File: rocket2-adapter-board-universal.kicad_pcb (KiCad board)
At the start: 2 copper layers, 45 x 55 mm, 13 parts, among them J2 Conn_01x04_Socket, J3 Conn_01x02_Socket, J4 Conn_01x04_Socket, J5 DSUB_15pin/VGA Veritical Fema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

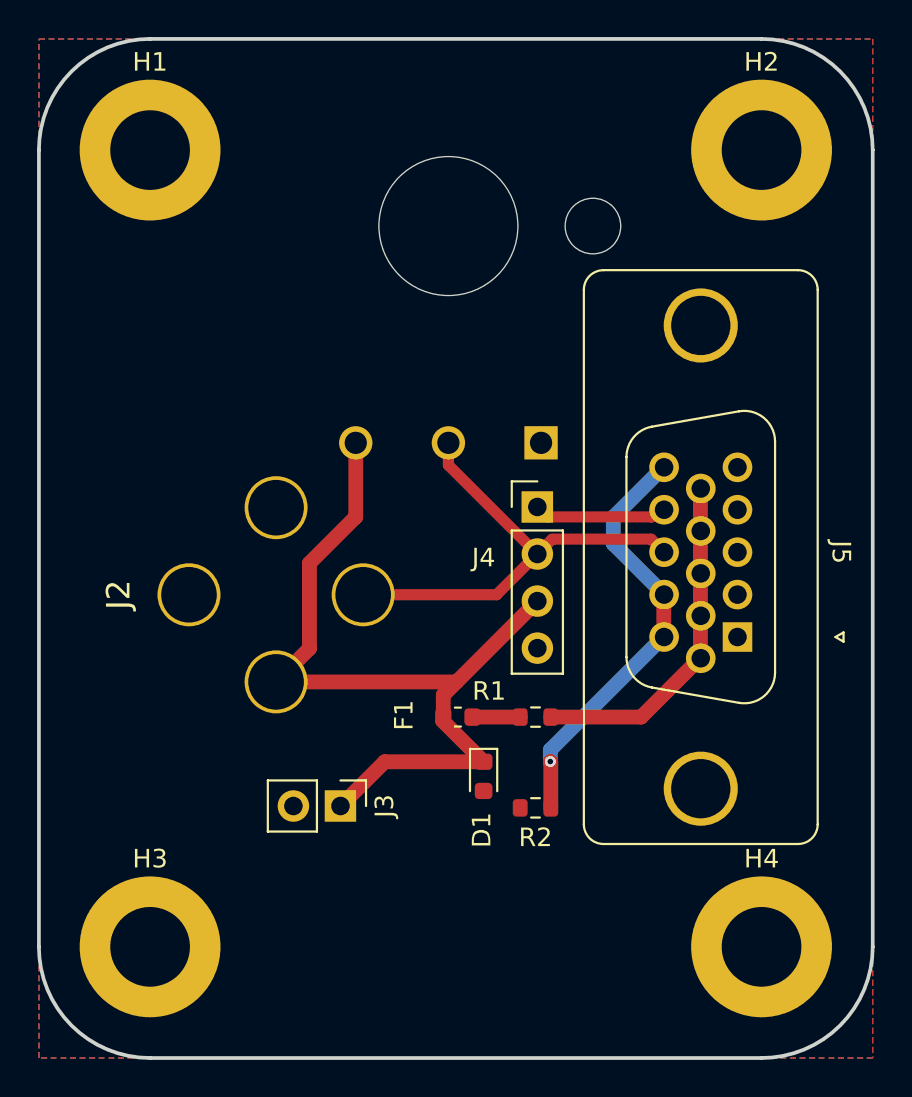
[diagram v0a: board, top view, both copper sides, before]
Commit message: Layout Update 2 + DSUB & Footprint Fixes
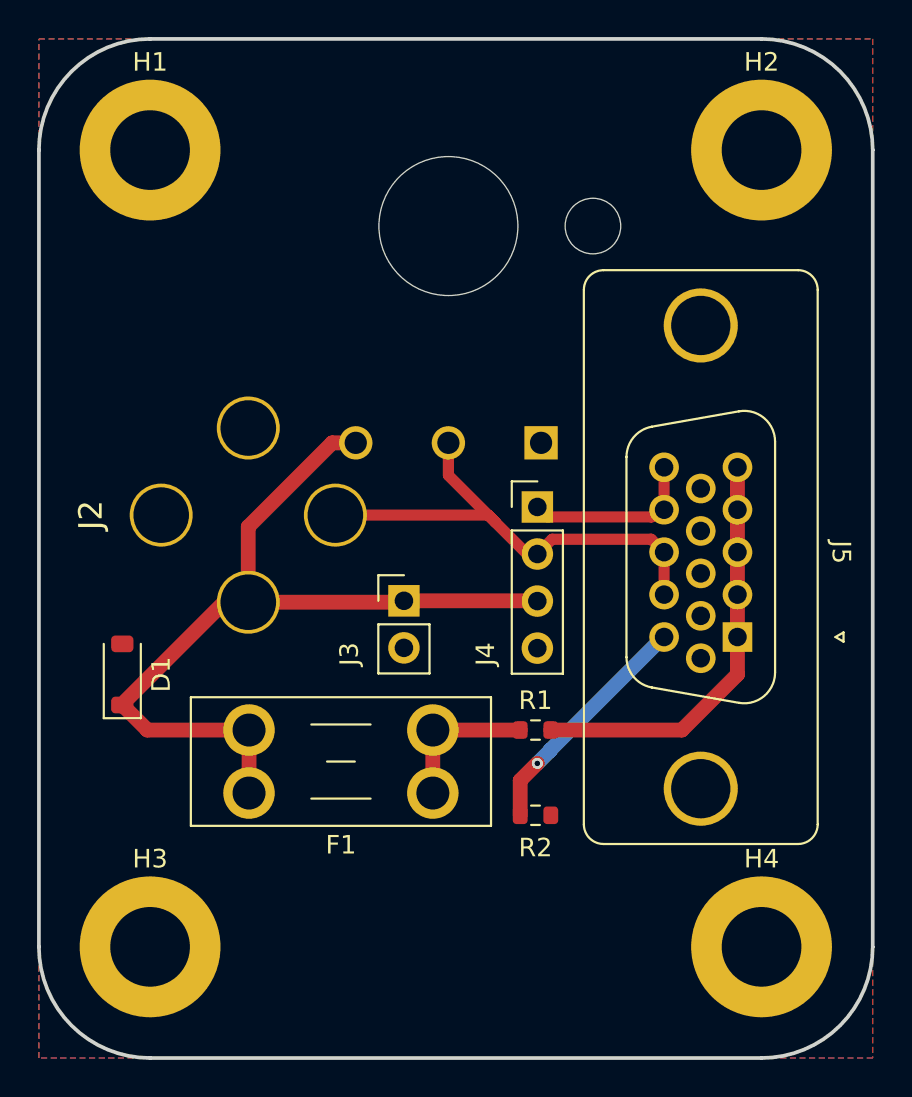
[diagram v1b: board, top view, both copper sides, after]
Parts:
- D1: footprint Diode_SMD:D_0603_1608Metric -> Diode_SMD:D_SOD-123
- F1: footprint Fuse:Fuse_0603_1608Metric -> Fuse:Fuseholder_Blade_Mini_Keystone_3568
- moved D1 20.3 mm to (124.5, 94.3), turned to 90 degrees
- moved J3 11.6 mm to (139.7, 90.3), turned to 0 degrees
- moved J2 4.55 mm to (131.3, 85.7)
- moved F1 4.32 mm to (141.3, 100.7)
- moved R1 0.70 mm to (146.8, 97.3)
- moved R2 0.40 mm to (146.8, 101.9), turned to 180 degrees
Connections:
- J5 pad 0: GND -> CHASSIS GND
- J5 pad 1: GND -> VIN
- J5 pad 10: VIN -> GND
- J5 pad 12: Net-(J5-Pad11) -> AIN+
- J5 pad 15: Net-(J5-Pad11) -> AIN-
- J5 pad 2: GND -> VIN
- J5 pad 3: GND -> VIN
- J5 pad 4: GND -> VIN
- J5 pad 5: GND -> VIN
- J5 pad 6: VIN -> GND
- J5 pad 7: VIN -> GND
- J5 pad 8: VIN -> GND
- J5 pad 9: VIN -> GND
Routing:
- net Net-(J5-Pad11): track 23.2 -> 12.9 mm
- net Net-(F1-Pad1): track 2.57 -> 8.15 mm
- net VIN: track 18.6 -> 22.5 mm
- net VBUS: track 44.8 -> 47.4 mm
- net AIN-: track 7.32 -> 9.61 mm
- net AIN+: track 25.9 -> 27.0 mm

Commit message: Layout Return Paths Fix
Streamlined GND return paths
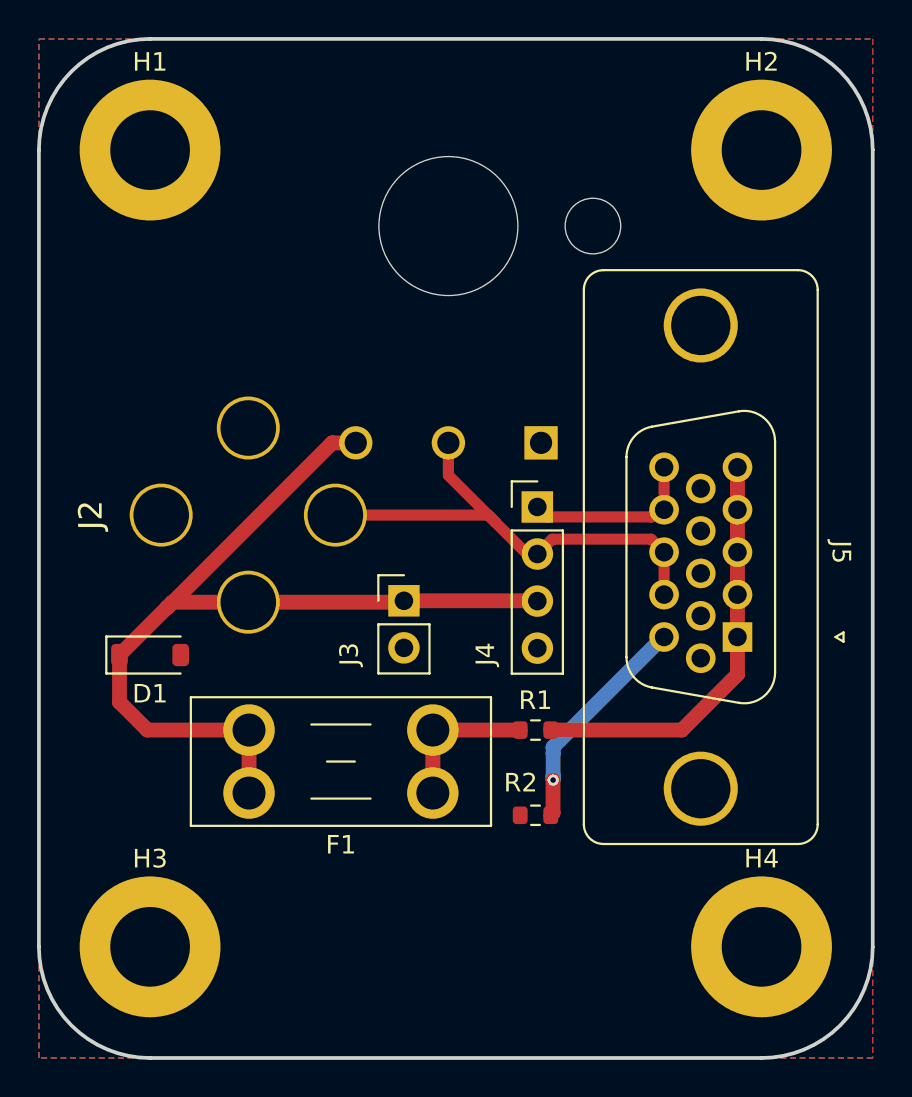
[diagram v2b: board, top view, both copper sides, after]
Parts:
- moved D1 1.83 mm to (126.0, 93.2), turned to 0 degrees
- turned R2 to 0 degrees
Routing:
- net VBUS: track 47.4 -> 51.2 mm

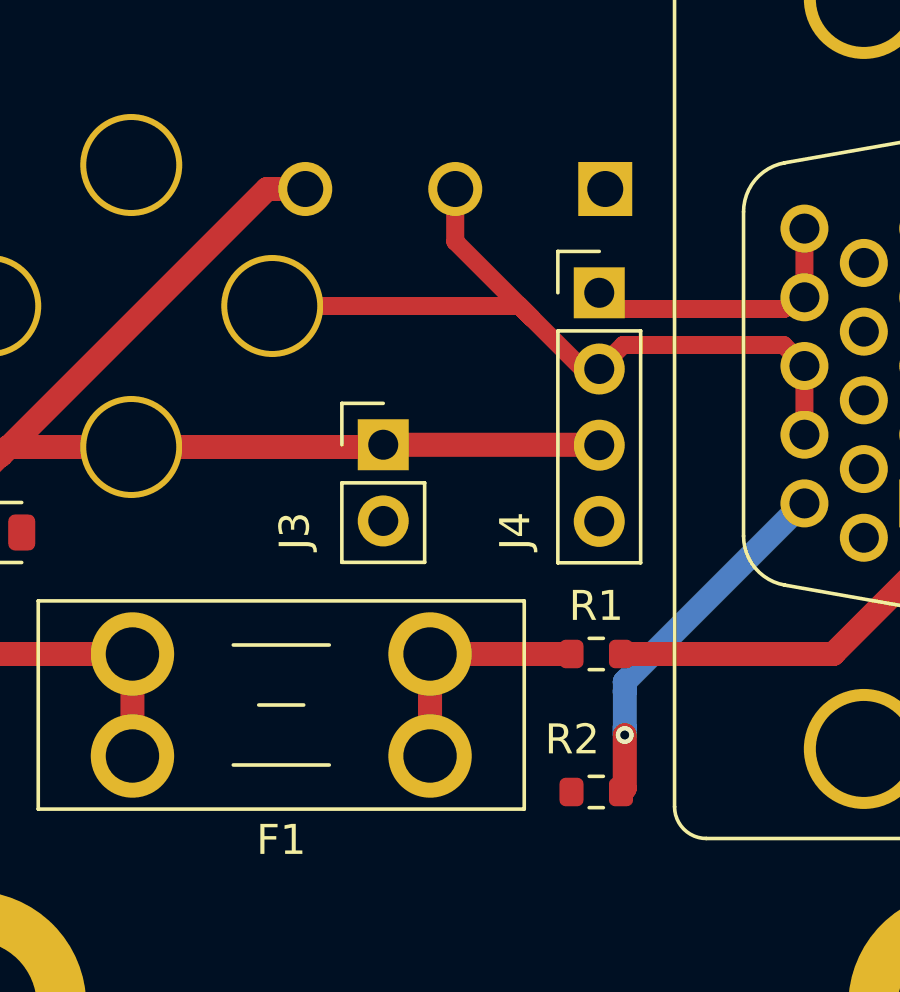
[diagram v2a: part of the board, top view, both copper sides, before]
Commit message: Layout Update 3 + Schematic Links & DSUB Update
Added R2 to bridge AIN+ and AIN-
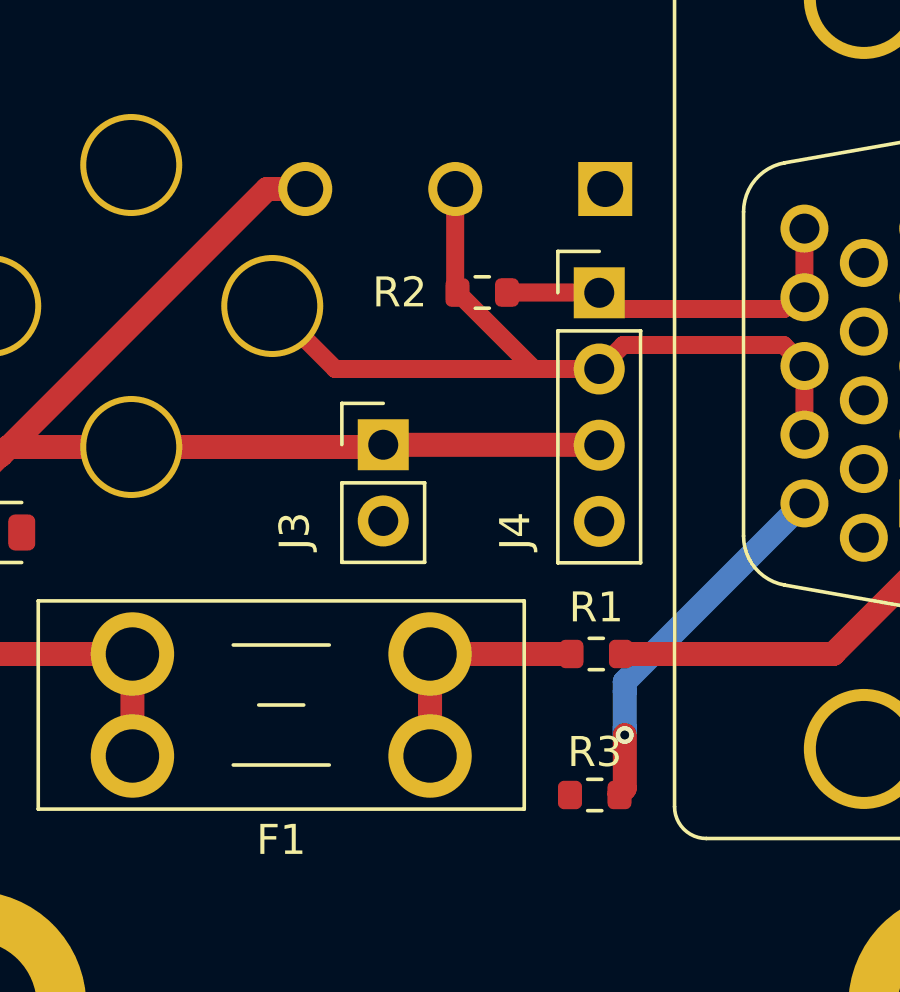
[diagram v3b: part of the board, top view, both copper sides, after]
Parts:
- added R3: 10k, Resistor_SMD:R_0603_1608Metric, F.Cu at (146.8, 102.0)
- R2: value 10k -> 0
- moved R2 17.1 mm to (143.0, 85.2), turned to 180 degrees
- turned R1 to 0 degrees
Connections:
- R1 pad 1: VIN -> Net-(F1-Pad1)
- R1 pad 2: Net-(F1-Pad1) -> VIN
- R2 pad 1: GND -> AIN-
- R2 pad 2: Net-(J5-Pad11) -> AIN+
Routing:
- net AIN+: track 27.0 -> 30.9 mm
- net AIN-: track 9.61 -> 12.7 mm

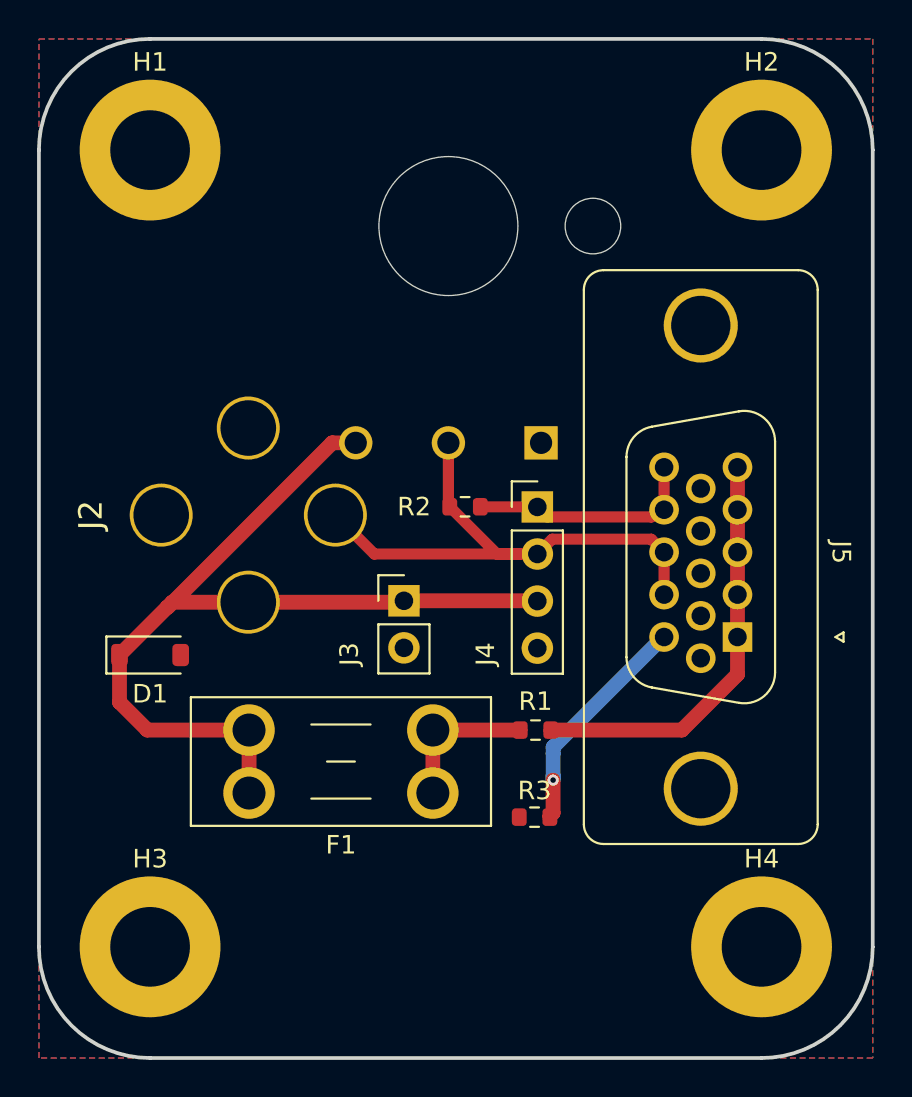
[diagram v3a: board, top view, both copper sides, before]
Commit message: Layout Update 4: NC pins, PT and Solenoid pad fixes
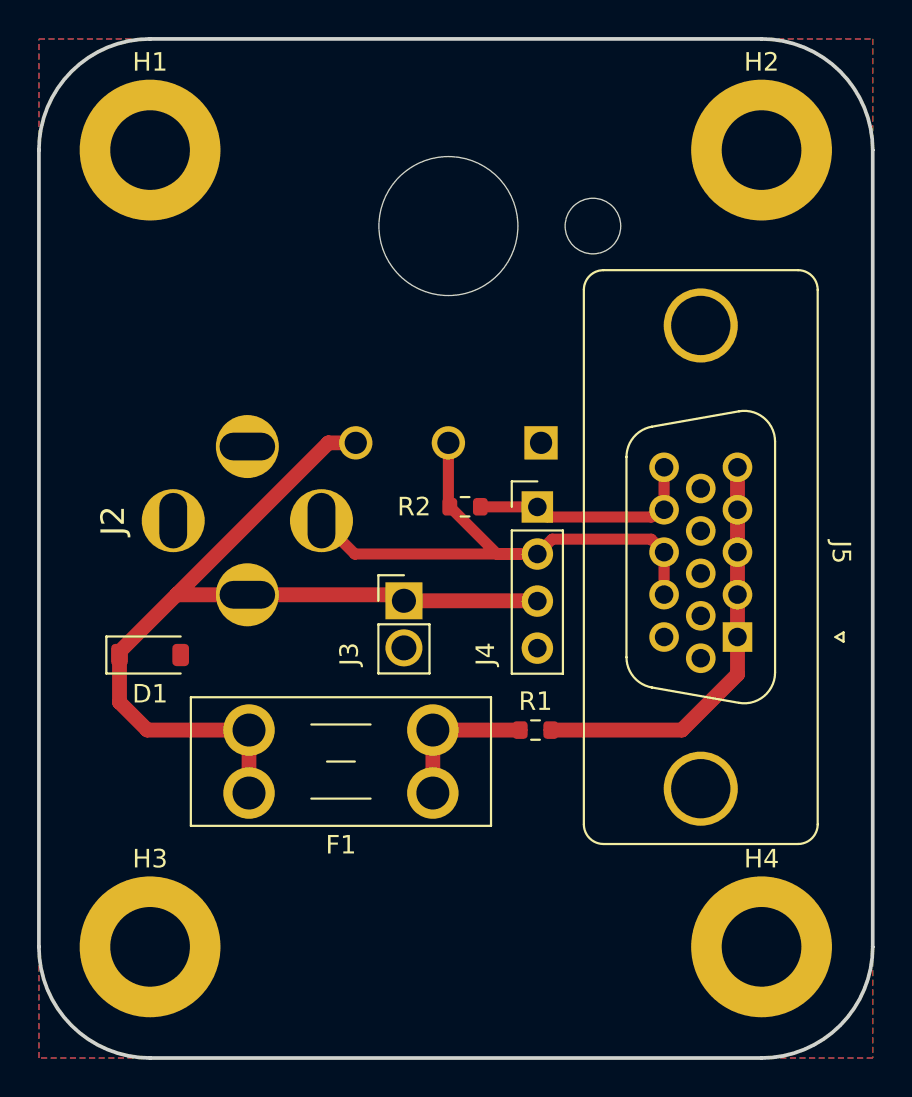
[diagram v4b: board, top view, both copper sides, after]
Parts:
- removed R3: 10k, Resistor_SMD:R_0603_1608Metric
- moved J2 0.30 mm to (131.2, 86.0)
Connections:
- J5 pad 0: CHASSIS GND -> unconnected-(J5-Pad0)
- J5 pad 11: Net-(J5-Pad11) -> unconnected-(J5-Pad11)
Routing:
- net Net-(J5-Pad11): track 12.5 -> 0.00 mm, vias 1 -> 0
- net AIN+: track 30.9 -> 31.5 mm

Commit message: Layout Update 5: Part spacing, Footprints, and Models
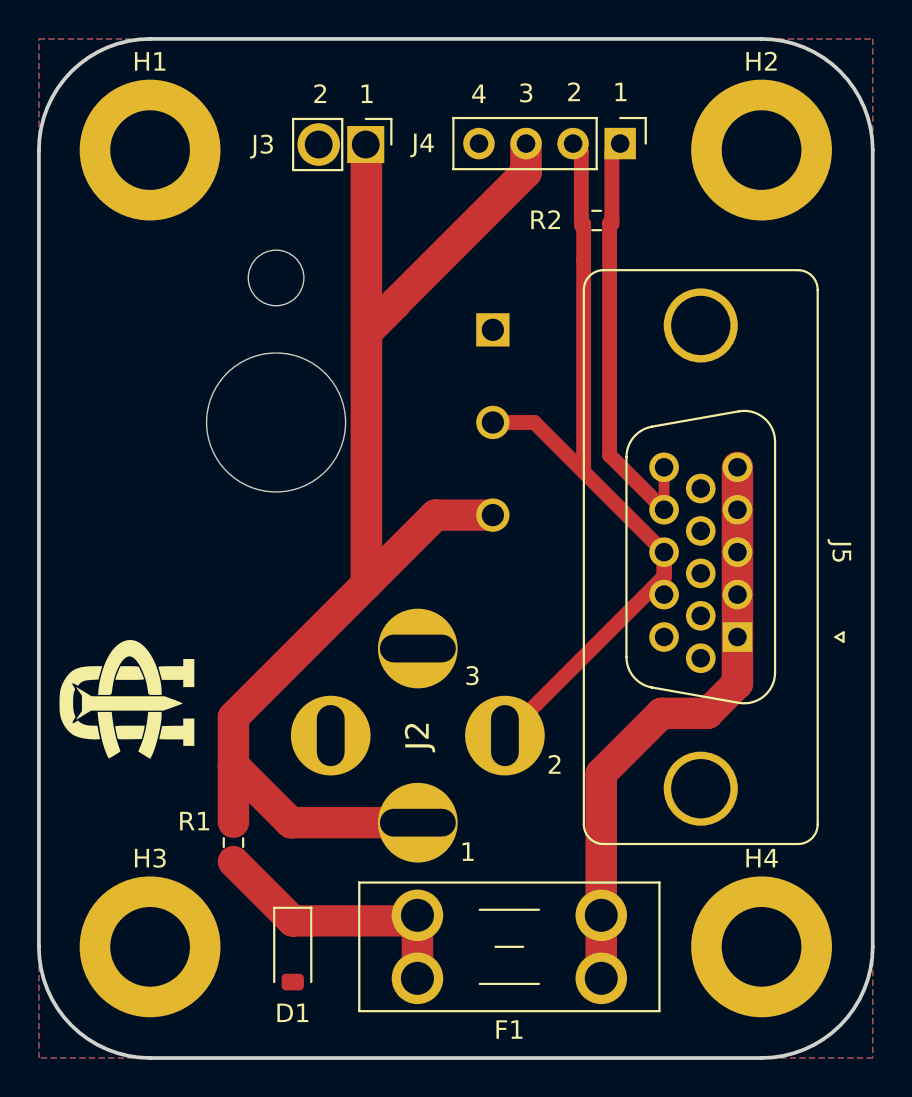
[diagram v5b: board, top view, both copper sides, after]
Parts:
- added G***: LOGO, UCIRP-KiCAD-Lib:PETER, B.Cu at (126.3, 94.5)
- added REF**: UCIRP_Logo_1, UCIRP-KiCAD-Lib:UCIRP_Logo_1, F.Cu at (124.9, 95.8)
- J3: footprint Connector_PinHeader_2.54mm:PinHeader_1x02_P2.54mm_Vertical -> UCIRP-KiCAD-Lib:Pad_Socket 16AWG_Solenoid_Wires
- moved J3 24.8 mm to (136.4, 65.7), turned to 180 degrees
- moved J4 20.1 mm to (151.4, 65.7), turned to -90 degrees
- moved D1 17.8 mm to (133.7, 109.2), turned to -90 degrees
- moved R1 17.4 mm to (130.5, 103.4), turned to -90 degrees
- moved R2 17.0 mm to (150.1, 69.8)
- moved J2 14.8 mm to (140.4, 97.6)
- moved F1 13.5 mm to (150.3, 110.7)
- moved VR1 6.63 mm to (144.5, 75.7), turned to -90 degrees
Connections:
- D1 pad 1: VBUS -> Net-(D1-K)
- F1 pad 1: Net-(F1-Pad1) -> VIN
- F1 pad 2: VBUS -> Net-(D1-K)
- R1 pad 1: Net-(F1-Pad1) -> VBUS
- R1 pad 2: VIN -> Net-(D1-K)
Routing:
- net VBUS: track 51.2 -> 73.0 mm
- net AIN+: track 31.5 -> 47.7 mm
- net Net-(D1-K): track 0.00 -> 14.8 mm
- net AIN-: track 12.7 -> 24.2 mm
- net VIN: track 22.5 -> 32.1 mm
- net Net-(F1-Pad1): track 8.15 -> 0.00 mm
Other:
- board text added: "1"
- board text added: "2"
- board text added: "3"
- board text added: "4"
